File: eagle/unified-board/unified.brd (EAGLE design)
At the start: 203.2 x 101.6 mm, 303 parts, among them IC101 THAT1512, IC201 THAT1512, IC301 THAT1512, IC401 THAT1512, J103 phantom, J104 eqout, J105 eqout, J203 phantom, J204 eqout, J205 eqout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

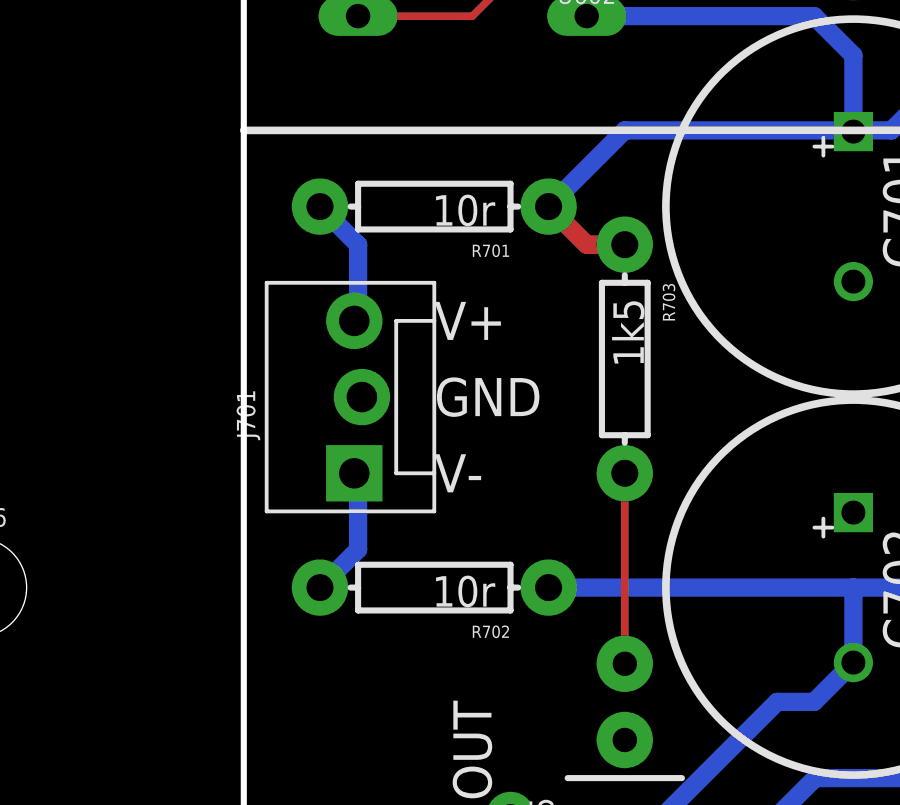
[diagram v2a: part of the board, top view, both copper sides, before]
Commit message: Some updates.
-More BOM detail
-SVG for temp panel.
-Few more dimensions on board.
-Tweaking preamp gains on rotpot boards.
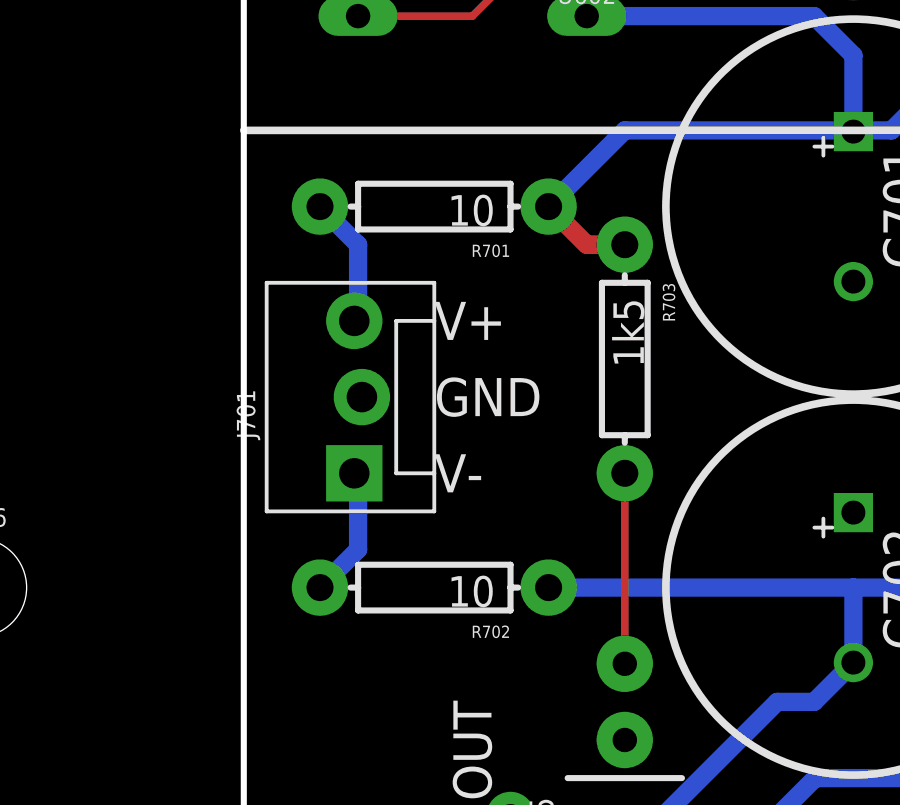
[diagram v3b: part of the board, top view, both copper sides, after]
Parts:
- R701, R702: value 10r -> 10
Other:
- board text added: "16x 8mm"
- board text added: "4x 9mm"
- board text removed: "16x ??"
- board text removed: "4x 10mm??"
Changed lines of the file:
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@@
 <layer number="19" name="Unrouted" color="6" fill="1" visible="yes" active="yes"/>
 <layer number="20" name="Dimension" color="15" fill="1" visible="yes" active="yes"/>
-<layer number="21" name="tPlace" color="16" fill="1" visible="no" active="yes"/>
-<layer number="22" name="bPlace" color="14" fill="1" visible="yes" active="yes"/>
+<layer number="21" name="tPlace" color="16" fill="1" visible="yes" active="yes"/>
+<layer number="22" name="bPlace" color="14" fill="1" visible="no" active="yes"/>
 <layer number="23" name="tOrigins" color="15" fill="1" visible="yes" active="yes"/>
-<layer number="24" name="bOrigins" color="15" fill="1" visible="yes" active="yes"/>
+<layer number="24" name="bOrigins" color="15" fill="1" visible="no" active="yes"/>
 <layer number="25" name="tNames" color="7" fill="1" visible="yes" active="yes"/>
 <layer number="26" name="bNames" color="7" fill="1" visible="no" active="yes"/>
@@
 <layer number="45" name="Holes" color="7" fill="1" visible="no" active="yes"/>
 <layer number="46" name="Milling" color="3" fill="1" visible="no" active="yes"/>
-<layer number="47" name="Measures" color="7" fill="1" visible="yes" active="yes"/>
+<layer number="47" name="Measures" color="7" fill="1" visible="no" active="yes"/>
 <layer number="48" name="Document" color="7" fill="1" visible="no" active="yes"/>
 <layer number="49" name="Reference" color="7" fill="1" visible="no" active="yes"/>
@@
 <dimension x1="181.61" y1="71.12" x2="241.3" y2="87.63" x3="252.73" y3="87.63" textsize="1.778" textratio="15" layer="47" dtype="leader" unit="inch"/>
 <dimension x1="181.61" y1="38.1" x2="243.84" y2="62.23" x3="252.73" y3="62.23" textsize="1.778" textratio="15" layer="47" dtype="leader" unit="inch"/>
-<text x="252.73" y="87.63" size="1.778" layer="47" font="vector" ratio="15">4x 10mm??</text>
-<text x="252.73" y="62.23" size="1.778" layer="47" font="vector" ratio="15">16x ??</text>
+<text x="252.73" y="87.63" size="1.778" layer="47" font="vector" ratio="15">4x 9mm</text>
+<text x="252.73" y="62.23" size="1.778" layer="47" font="vector" ratio="15">16x 8mm</text>
+<dimension x1="0" y1="101.6" x2="0" y2="92.71" x3="-7.62" y3="97.155" textsize="1.778" textratio="15" layer="47" unit="inch"/>
+<dimension x1="0" y1="101.6" x2="0" y2="67.31" x3="-11.43" y3="84.455" textsize="1.778" textratio="15" layer="47" unit="inch"/>
+<dimension x1="12.7" y1="45.72" x2="0" y2="45.72" x3="6.35" y3="105.41" textsize="1.778" textratio="15" layer="47" unit="inch"/>
+<dimension x1="12.7" y1="45.72" x2="12.7" y2="101.6" x3="-16.51" y3="73.66" textsize="1.778" textratio="15" layer="47" unit="inch"/>
 </plain>
 <attributes>
@@
 <attribute name="SF_ID" value="PRT-08096" x="31.75" y="53.34" size="1.778" layer="27" font="vector" ratio="15" rot="R90" display="off"/>
 </element>
-<element name="R701" library="SparkFun-Resistors" package="AXIAL-0.3" value="10r" x="6.35" y="62.23" rot="R180"/>
-<element name="R702" library="SparkFun-Resistors" package="AXIAL-0.3" value="10r" x="6.35" y="49.53" rot="R180"/>
+<element name="R701" library="SparkFun-Resistors" package="AXIAL-0.3" value="10" x="6.35" y="62.23" rot="R180"/>
+<element name="R702" library="SparkFun-Resistors" package="AXIAL-0.3" value="10" x="6.35" y="49.53" rot="R180"/>
 <element name="R703" library="SparkFun-Resistors" package="AXIAL-0.3" value="1k5" x="12.7" y="57.15" rot="R270"/>
 <element name="D701" library="SparkFun-LED" package="LED_5MM" value="" x="12.7" y="45.72" rot="MR270"/>

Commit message: Many changes from checkplots.
Some footprints were incorrect.  Library, board & schem all updated.
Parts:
- removed H606, H607, H608, H609, H610: STAND-OFF, SparkFun-Hardware:STAND-OFF
- C107, C108, C207, C208, C307, C308, C407, C408: device mixer:CAP-PANA-5LS-6DIAM -> mixer:CAP-PANA-2LS-6DIAM
- C109, C110, C114, C120, C209, C210, C214, C220, C309, C310, C314, C320, C409, C410, C414, C420, C502, C602: device mixer:CAP-PANA-5LS-5DIAM -> mixer:CAP-PANA-2LS-5DIAM
- moved C605 5.68 mm to (3.81, 38.1), turned to 180 degrees
- moved C505 5.68 mm to (29.2, 38.1), turned to 180 degrees
- moved C214 5.08 mm to (144.8, 31.8)
- moved C314 5.08 mm to (106.7, 31.8)
- moved C414 5.08 mm to (68.6, 31.8)
- moved C114 5.08 mm to (182.9, 31.8)
- moved R507 2.84 mm to (47.0, 22.9)
- moved R607 2.84 mm to (21.6, 22.9)
- moved C502 2.54 mm to (29.2, 30.5)
- moved C602 2.54 mm to (5.08, 30.5)
- moved FB501 2.54 mm to (44.5, 35.6)
- moved FB601 2.54 mm to (19.1, 35.6)
- moved C120 1.27 mm to (168.9, 11.4)
- moved C220 1.27 mm to (130.8, 11.4)
- moved C320 1.27 mm to (92.7, 11.4)
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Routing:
- net VCC: track 616.2 -> 627.7 mm
- net N$146: track 90.0 -> 80.8 mm
- net N$82: track 90.0 -> 80.8 mm
- net N$30: track 90.0 -> 80.8 mm
- net N$114: track 90.0 -> 80.8 mm
- net N$11: track 29.6 -> 34.0 mm
- net N$20: track 37.2 -> 33.6 mm
- net N$85: track 37.2 -> 33.6 mm
- net N$117: track 37.2 -> 33.6 mm
- net PREOUT: track 37.2 -> 33.6 mm
- net N$152: track 30.9 -> 34.3 mm
- net VNEG: track 562.8 -> 565.0 mm
- net N$7: track 14.7 -> 16.6 mm
- net N$151: track 14.7 -> 16.6 mm
- net N$6: track 55.6 -> 57.5 mm
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
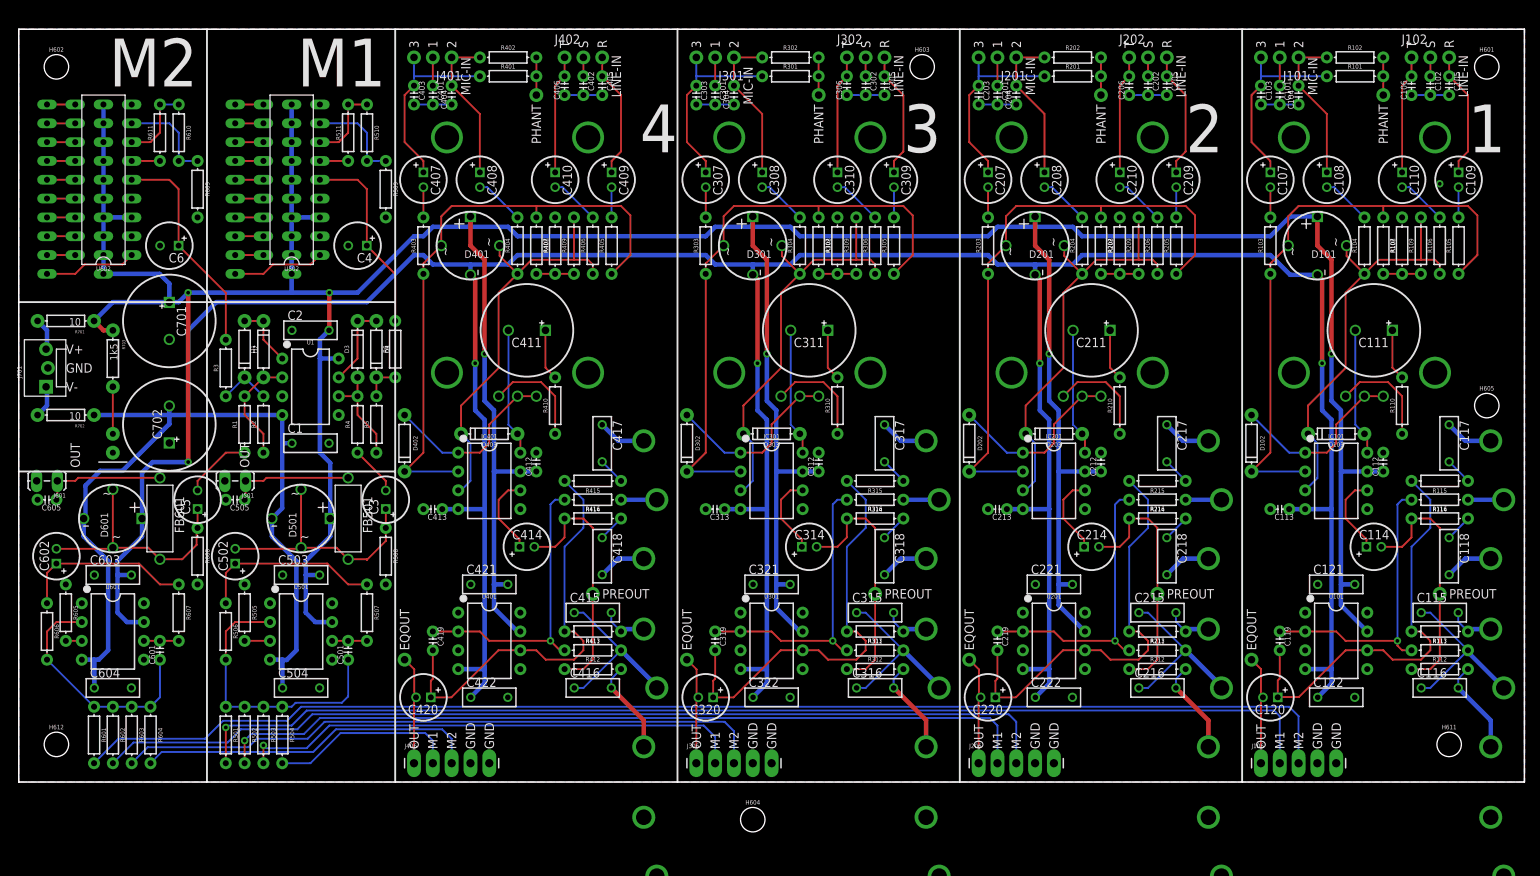
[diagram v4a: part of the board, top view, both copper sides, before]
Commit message: Peppered the board with ground stitch vias.
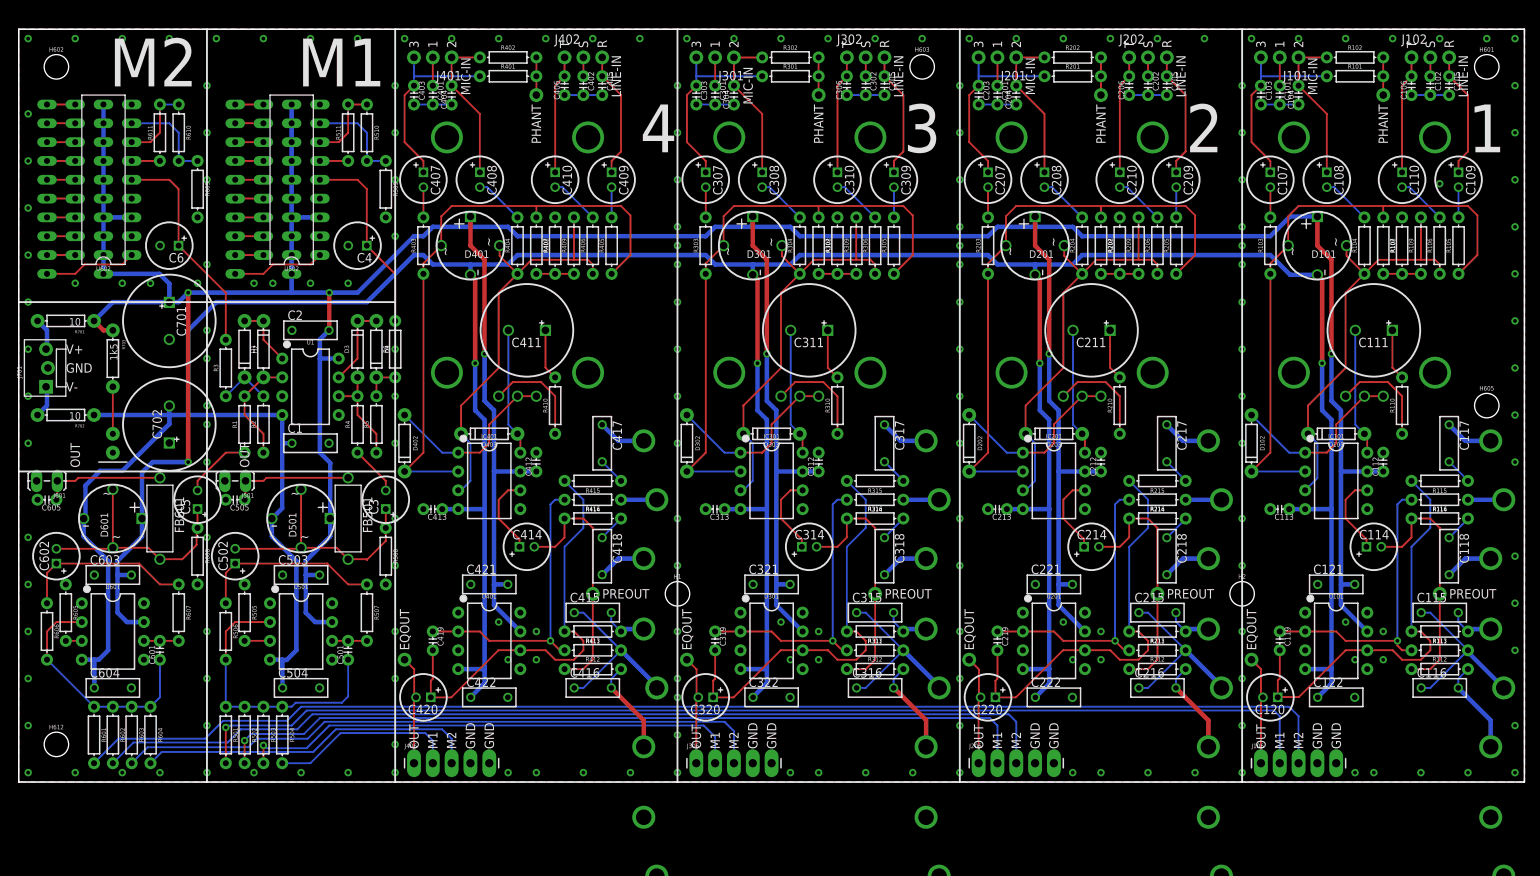
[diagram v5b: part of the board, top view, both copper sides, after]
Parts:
- removed H604, H611: STAND-OFF, SparkFun-Hardware:STAND-OFF
- added H1, H2: STAND-OFF, SparkFun-Hardware:STAND-OFF

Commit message: Board touchups before gerbers.
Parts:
- removed VR104, VR105, VR204, VR205, VR304, VR305, VR404, VR405: 10K, mixer:ALPHA-RV24AF40-POT
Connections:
- net GND: no longer VR104.CCW, VR105.CCW, VR204.CCW, VR205.CCW, VR304.CCW, VR305.CCW, VR404.CCW, VR405.CCW
